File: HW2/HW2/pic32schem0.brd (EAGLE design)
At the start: 50 x 50 mm, 21 parts, among them J3 USB-MB-H

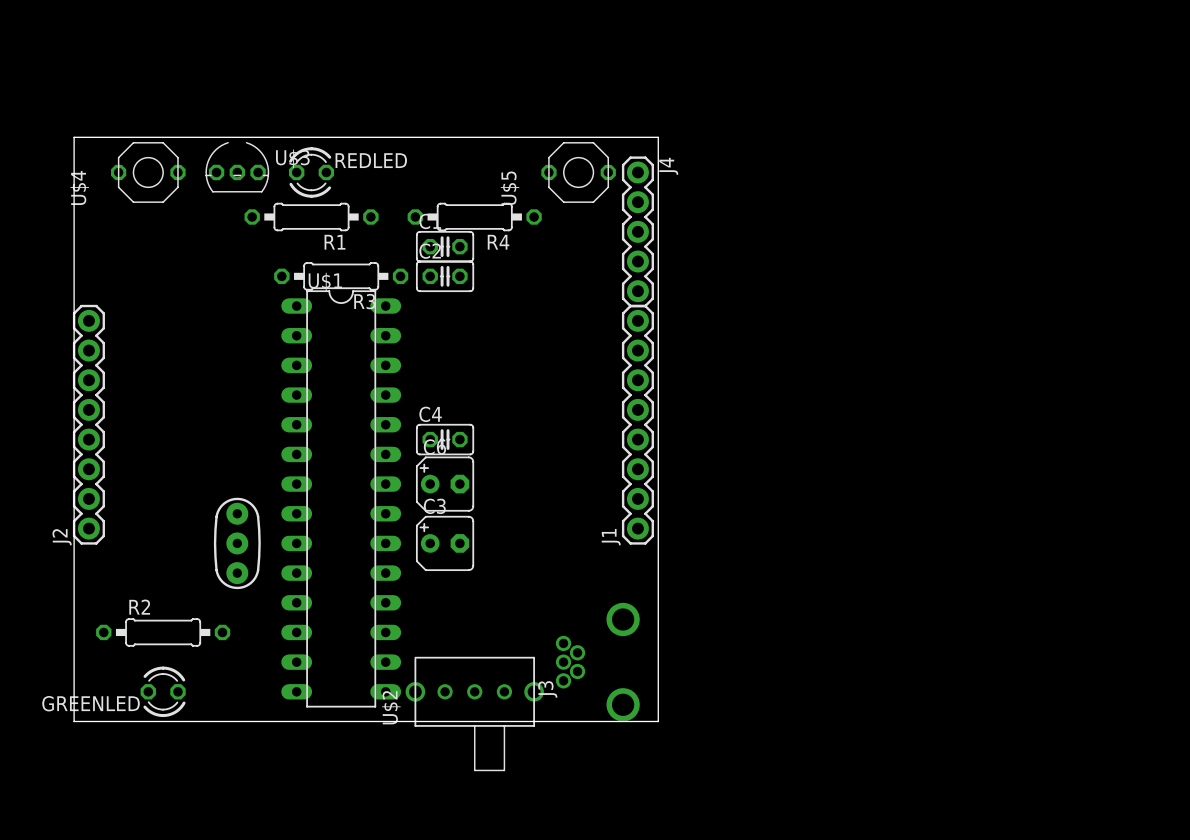
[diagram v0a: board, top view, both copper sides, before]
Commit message: Scrapped original pcb, got ground plane to work
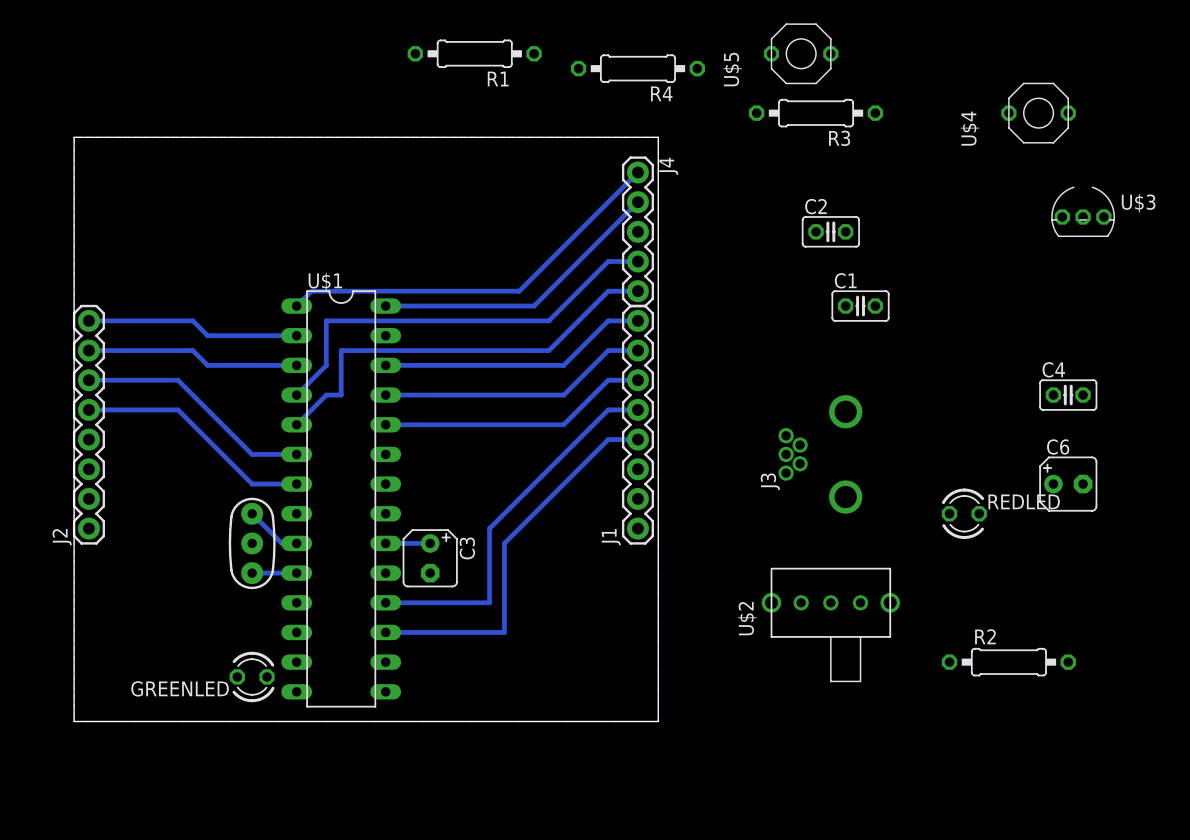
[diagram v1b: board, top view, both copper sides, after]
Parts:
- moved U$4 76.4 mm to (85.1, 52.1)
- moved U$3 72.5 mm to (86.4, 43.2)
- moved R2 72.4 mm to (80.0, 5.08)
- moved REDLED 63.1 mm to (76.2, 17.8)
- moved C4 53.5 mm to (85.1, 27.9)
- moved C6 53.3 mm to (85.1, 20.3)
- moved R3 43.0 mm to (63.5, 52.1)
- moved C1 35.9 mm to (67.3, 35.6)
- moved C2 33.2 mm to (64.8, 41.9)
- moved U$2 31.4 mm to (64.8, 10.2)
- moved J3 26.1 mm to (66.0, 22.9)
- moved U$5 21.6 mm to (64.8, 57.1)
- moved R1 19.8 mm to (34.3, 57.1)
- moved R4 18.9 mm to (48.3, 55.9)
- moved GREENLED 7.73 mm to (15.2, 3.81)
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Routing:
- net PGD: track 0.00 -> 36.2 mm
- net PGC: track 0.00 -> 36.2 mm
- net MCLR: track 0.00 -> 33.9 mm
- net B8: track 0.00 -> 32.9 mm
- net B9: track 0.00 -> 32.1 mm
- net +3V3: track 0.00 -> 25.3 mm
- net B15: track 0.00 -> 23.2 mm
- net B14: track 0.00 -> 23.2 mm
- net B13: track 0.00 -> 23.2 mm
- net B3: track 0.00 -> 20.4 mm
- net B2: track 0.00 -> 20.4 mm
- net A1: track 0.00 -> 18.3 mm
- net A0: track 0.00 -> 18.3 mm
- net N$2: track 0.00 -> 4.86 mm
- net N$1: track 0.00 -> 3.81 mm
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- added copper zone on layer 16, net GND

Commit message: Finished pcb, quite a few errors
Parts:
- moved U$4 89.8 mm to (6.35, 8.89)
- moved R3 69.4 mm to (6.35, 12.7)
- moved R2 68.6 mm to (11.4, 2.54)
- moved J3 65.9 mm to (3.81, 44.5), turned to 0 degrees
- moved C1 61.4 mm to (14.0, 5.08), turned to 180 degrees
- moved U$2 60.7 mm to (16.5, 47.0), turned to 180 degrees
- moved C6 59.9 mm to (29.2, 41.9), turned to 270 degrees
- moved REDLED 57.5 mm to (26.7, 47.0), turned to 180 degrees
- moved U$3 53.5 mm to (33.0, 47.0), turned to 180 degrees
- moved C4 50.6 mm to (36.8, 43.2)
- moved C2 36.4 mm to (29.2, 34.3), turned to 270 degrees
- moved R4 35.9 mm to (34.3, 22.9)
- moved U$5 28.5 mm to (38.1, 47.0), turned to 180 degrees
- moved R1 21.6 mm to (20.3, 40.6), turned to 0 degrees
- moved GREENLED 11.4 mm to (3.81, 3.81), turned to 270 degrees
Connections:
- removed net A1/LED: GREENLED.A, U$1.12
- removed net A4: J2.3
- removed net B4: J2.4
- removed net N$7: J1.3
- new net A4/LED: GREENLED.A, J2.3, U$1.12
- net B4/USER: now also J2.4
- net B7: now also J1.3
- net GND: now also U$2.4.OUT; no longer U$2.2.OUT
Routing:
- net +3V3: track 25.3 -> 105.8 mm, vias 0 -> 1
- net D-: track 0.00 -> 50.5 mm, vias 0 -> 1
- net D+: track 0.00 -> 40.3 mm
- net +5V: track 0.00 -> 34.4 mm
- net B7: track 0.00 -> 33.6 mm
- net B4/USER: track 0.00 -> 22.0 mm
- net A4/LED: track 0.00 -> 16.3 mm
- net N$3: track 0.00 -> 13.5 mm
- net N$5: track 0.00 -> 12.4 mm
- net N$6: track 0.00 -> 10.2 mm
- net MCLR: track 33.9 -> 41.6 mm, vias 0 -> 1
- net N$8: track 0.00 -> 2.54 mm
- net PGD: track 36.2 -> 34.4 mm
- net PGC: track 36.2 -> 34.4 mm
